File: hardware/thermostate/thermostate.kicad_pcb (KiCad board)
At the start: 2 copper layers, 80 x 80 mm, 28 parts, among them IC1 L8050QLT1G, IC2 L8050QLT1G, P1 USB_C_Plug_USB2.0, SW1 SW_Push, SW2 SW_Push, U1 ESP32-S3-WROOM-1, U2 LM1117-3.3

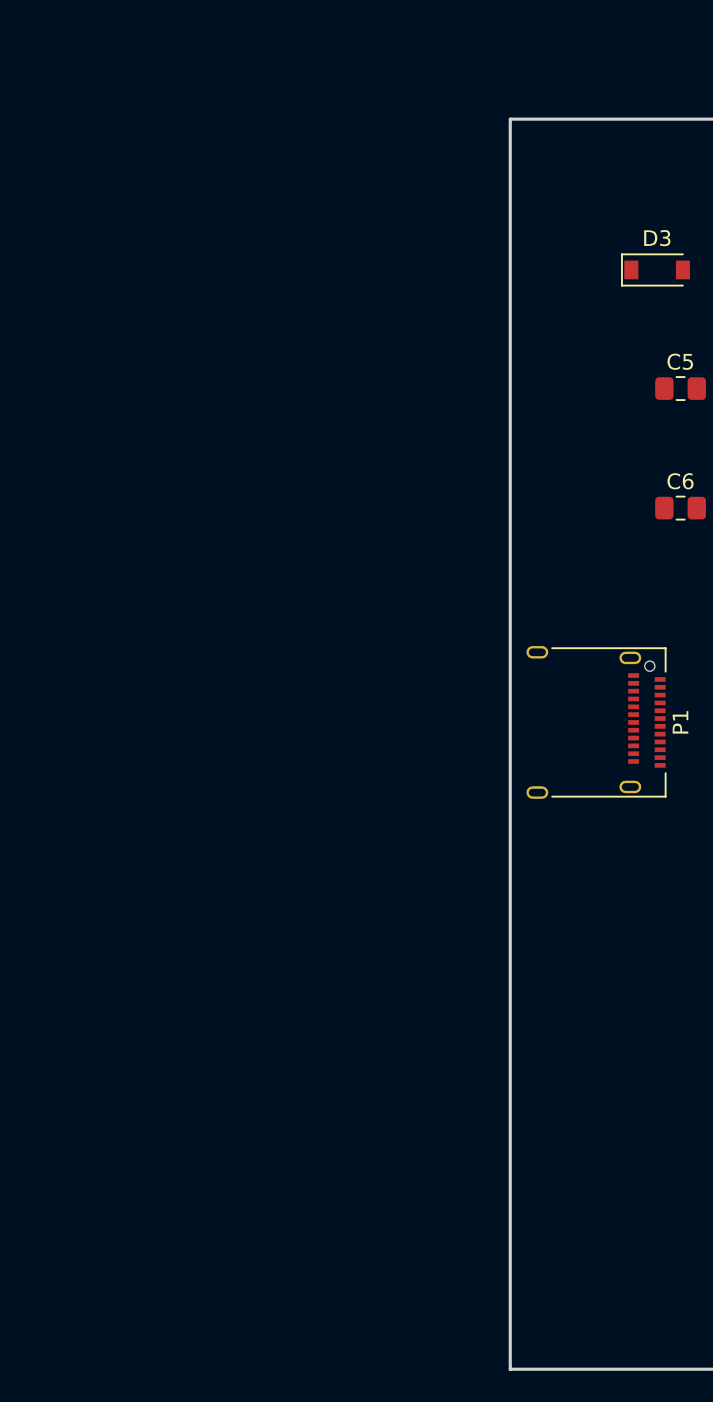
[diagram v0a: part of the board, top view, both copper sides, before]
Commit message: Add temperature sensor
Signed-off-by: Javier <javierfernandezvillasante@gmail.com>
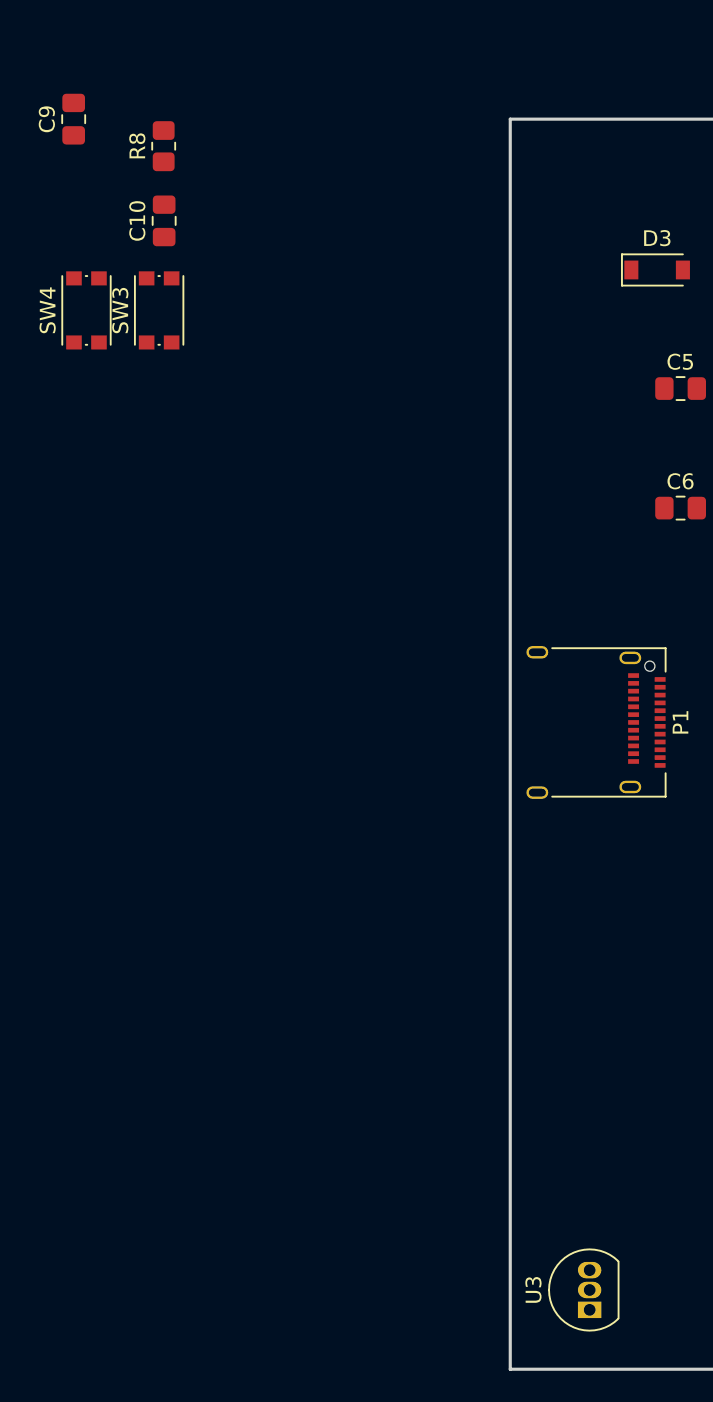
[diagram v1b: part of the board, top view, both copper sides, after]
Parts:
- added C10: 0.1uF/50V(20%), Capacitor_SMD:C_0805_2012Metric_Pad1.18x1.45mm_HandSolder, F.Cu at (84.5, 59.9)
- added C9: 0.1uF/50V(20%), Capacitor_SMD:C_0805_2012Metric_Pad1.18x1.45mm_HandSolder, F.Cu at (78.7, 53.3)
- added R8: 4K7(20%), Resistor_SMD:R_0805_2012Metric_Pad1.20x1.40mm_HandSolder, F.Cu at (84.5, 55.1)
- added SW3: SW_Push, Button_Switch_SMD:SW_Push_1P1T_NO_CK_KMR2, F.Cu at (84.2, 65.6)
- added SW4: SW_Push, Button_Switch_SMD:SW_Push_1P1T_NO_CK_KMR2, F.Cu at (79.6, 65.6)
- added U3: DS18B20, Package_TO_SOT_THT:TO-92_Inline, F.Cu at (111.8, 129.5)
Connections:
- net GND renamed PAD_-_ExternalPush_1
- U1 pad 16: unconnected-(U1-Pad16) -> TemperatureSensor
- U1 pad 23: unconnected-(U1-Pad23) -> ExternalPush_1
- U1 pad 26: unconnected-(U1-Pad26) -> ExternalPush_2

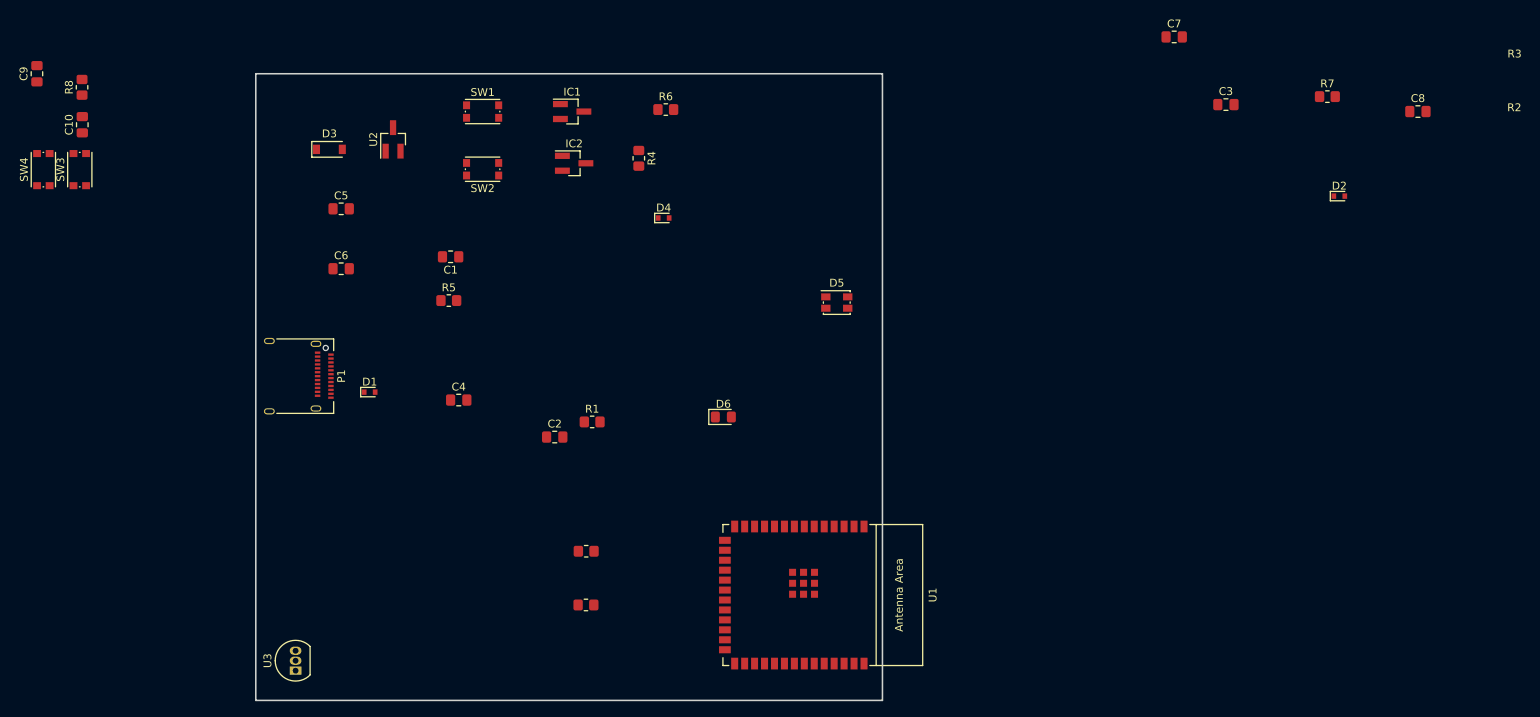
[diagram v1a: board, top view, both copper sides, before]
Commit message: Add Components PCB
Signed-off-by: Javier <javierfernandezvillasante@gmail.com>
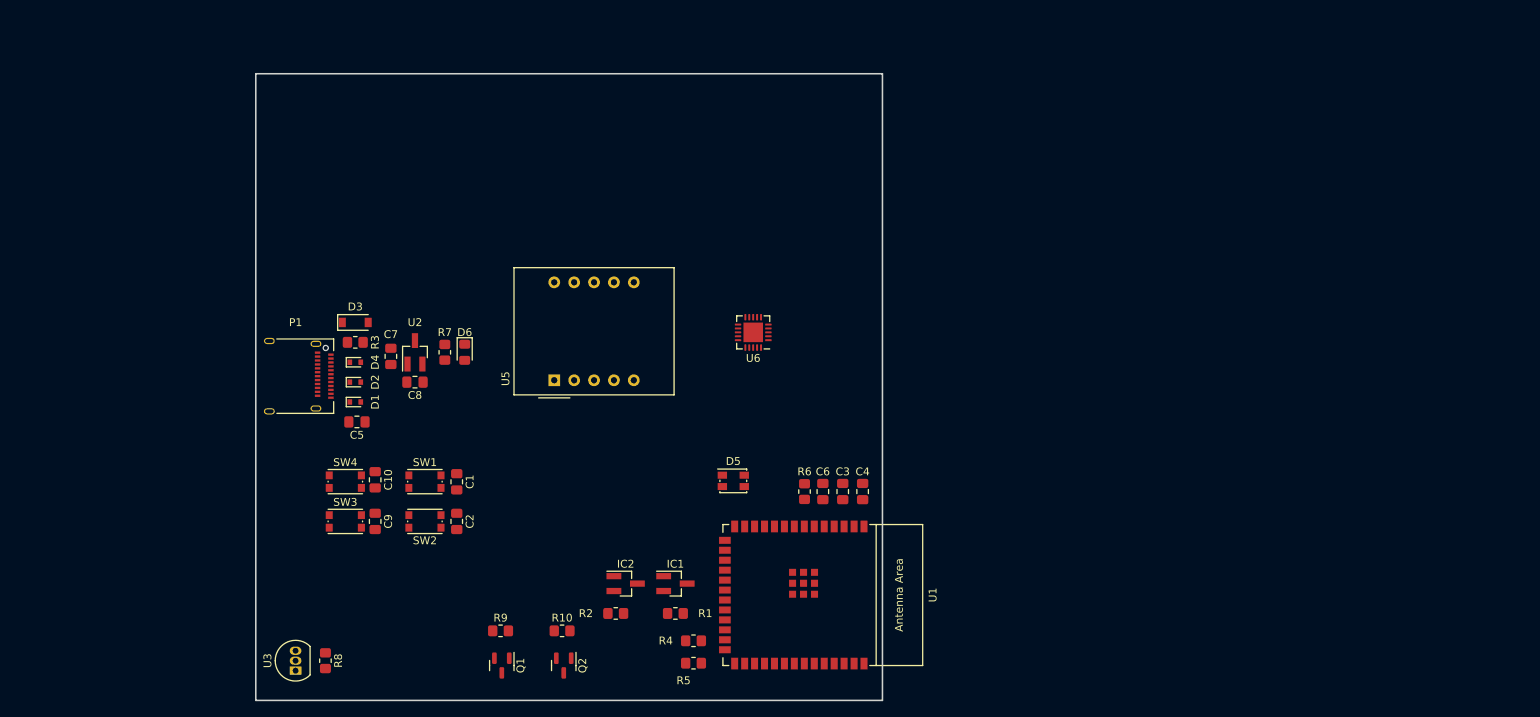
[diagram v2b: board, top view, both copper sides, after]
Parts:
- added Q1: BC847, Package_TO_SOT_SMD:SOT-23, F.Cu at (138.1, 128.9)
- added Q2: BC847, Package_TO_SOT_SMD:SOT-23, F.Cu at (146.0, 128.9)
- added R10: 10k (1%), Resistor_SMD:R_0805_2012Metric_Pad1.20x1.40mm_HandSolder, F.Cu at (145.8, 124.5)
- added R9: 10k (1%), Resistor_SMD:R_0805_2012Metric_Pad1.20x1.40mm_HandSolder, F.Cu at (137.9, 124.5)
- added U5: ELD-426SYGWA, Display_7Segment:ELD_426XXXX, F.Cu at (144.8, 92.5)
- added U6: ULN2803A, Package_DFN_QFN:QFN-20-1EP_4x4mm_P0.5mm_EP2.5x2.5mm, F.Cu at (170.2, 86.4)
- moved C8 132.6 mm to (127.0, 92.7), turned to 180 degrees
- moved D2 127.8 mm to (119.4, 92.7)
- moved R7 117.3 mm to (130.8, 88.9), turned to -90 degrees
- moved C7 108.0 mm to (123.9, 89.4), turned to -90 degrees
- moved R8 79.5 mm to (115.6, 128.3), turned to -90 degrees
- moved C9 71.6 mm to (121.9, 110.5), turned to -90 degrees
- moved C3 69.5 mm to (181.6, 106.7), turned to 90 degrees
- moved C6 67.8 mm to (179.1, 106.7), turned to 90 degrees
- moved R4 62.0 mm to (162.6, 125.7), turned to 180 degrees
- moved IC1 61.7 mm to (160.2, 118.4)
- moved C10 58.8 mm to (121.9, 105.2), turned to -90 degrees
- moved SW3 56.3 mm to (118.1, 110.5), turned to 0 degrees
- moved R5 55.8 mm to (162.6, 128.6), turned to 180 degrees
- moved SW4 55.4 mm to (118.1, 105.4), turned to 0 degrees
- moved IC2 54.1 mm to (153.9, 118.4)
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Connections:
- U1 pad 10: unconnected-(U1-Pad10) -> 7SEG_G
- U1 pad 11: unconnected-(U1-Pad11) -> 7SEG_DP
- U1 pad 19: unconnected-(U1-Pad19) -> 7SEG_A
- U1 pad 20: unconnected-(U1-Pad20) -> 7SEG_B
- U1 pad 21: unconnected-(U1-Pad21) -> 7SEG_C
- U1 pad 22: unconnected-(U1-Pad22) -> 7SEG_D
- U1 pad 36: unconnected-(U1-Pad36) -> 7SEG_2Controller
- U1 pad 37: unconnected-(U1-Pad37) -> 7SEG_1Controller
- U1 pad 8: unconnected-(U1-Pad8) -> 7SEG_E
- U1 pad 9: unconnected-(U1-Pad9) -> 7SEG_F

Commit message: Start desing PCB
Signed-off-by: Javier <javierfernandezvillasante@gmail.com>
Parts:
- added J1: Conn_01x02_Male, TerminalBlock_MetzConnect:TerminalBlock_MetzConnect_360291_1x01_Horizontal_ScrewM3.0_Boxed, F.Cu at (234.9, 45.7)
- added J2: Conn_01x02_Male, TerminalBlock_MetzConnect:TerminalBlock_MetzConnect_360291_1x01_Horizontal_ScrewM3.0_Boxed, F.Cu at (246.0, 45.7)
- added K1: SRD-03VDC-SL-C, SRD-03VDC-SL-C:SRD03VDCSLC, F.Cu at (214.2, 39.6)
- added R11: RK09K1130A5R, RK09K1130A5R:RK09K1130A5R, F.Cu at (240.0, 31.3)
- moved R4 22.6 mm to (174.7, 106.7), turned to 90 degrees
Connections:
- net GPIO19 renamed /ESP32_minimal/USB_N
- net GPIO20 renamed /ESP32_minimal/USB_P
- C1 pad 1: PAD_-_ExternalPush_1 -> GND
- C10 pad 1: PAD_-_ExternalPush_1 -> GND
- C2 pad 1: PAD_-_ExternalPush_1 -> GND
- C3 pad 2: PAD_-_ExternalPush_1 -> GND
- C4 pad 2: PAD_-_ExternalPush_1 -> GND
- C5 pad 2: PAD_-_ExternalPush_1 -> GND
- C6 pad 2: PAD_-_ExternalPush_1 -> GND
- C7 pad 2: PAD_-_ExternalPush_1 -> GND
- C8 pad 2: PAD_-_ExternalPush_1 -> GND
- C9 pad 1: PAD_-_ExternalPush_1 -> GND
- D1 pad 1: PAD_-_ExternalPush_1 -> GND
- D2 pad 1: PAD_-_ExternalPush_1 -> GND
- D4 pad 1: PAD_-_ExternalPush_1 -> GND
- D5 pad 2: PAD_-_ExternalPush_1 -> GND
- D6 pad 1: PAD_-_ExternalPush_1 -> GND
- P1 pad A1: PAD_-_ExternalPush_1 -> GND
- P1 pad A12: PAD_-_ExternalPush_1 -> GND
- P1 pad B1: PAD_-_ExternalPush_1 -> GND
- P1 pad B12: PAD_-_ExternalPush_1 -> GND
- P1 pad S1: PAD_-_ExternalPush_1 -> GND
- R3 pad 2: PAD_-_ExternalPush_1 -> GND
- SW1 pad 1: PAD_-_ExternalPush_1 -> GND
- SW2 pad 1: PAD_-_ExternalPush_1 -> GND
- SW3 pad 1: PAD_-_ExternalPush_1 -> ExternalPush_1
- SW4 pad 1: PAD_-_ExternalPush_1 -> Net-(SW4-Pad1)
- U1 pad 1: PAD_-_ExternalPush_1 -> GND
- U1 pad 40: PAD_-_ExternalPush_1 -> GND
- U1 pad 41: PAD_-_ExternalPush_1 -> GND
- U2 pad 1: PAD_-_ExternalPush_1 -> GND
- U3 pad 1: PAD_-_ExternalPush_1 -> GND
- U6 pad 9: PAD_-_ExternalPush_1 -> GND
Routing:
- net DTR: track 0.00 -> 12.7 mm
- net RTS: track 0.00 -> 6.30 mm
- net GPIO0: track 0.00 -> 4.28 mm

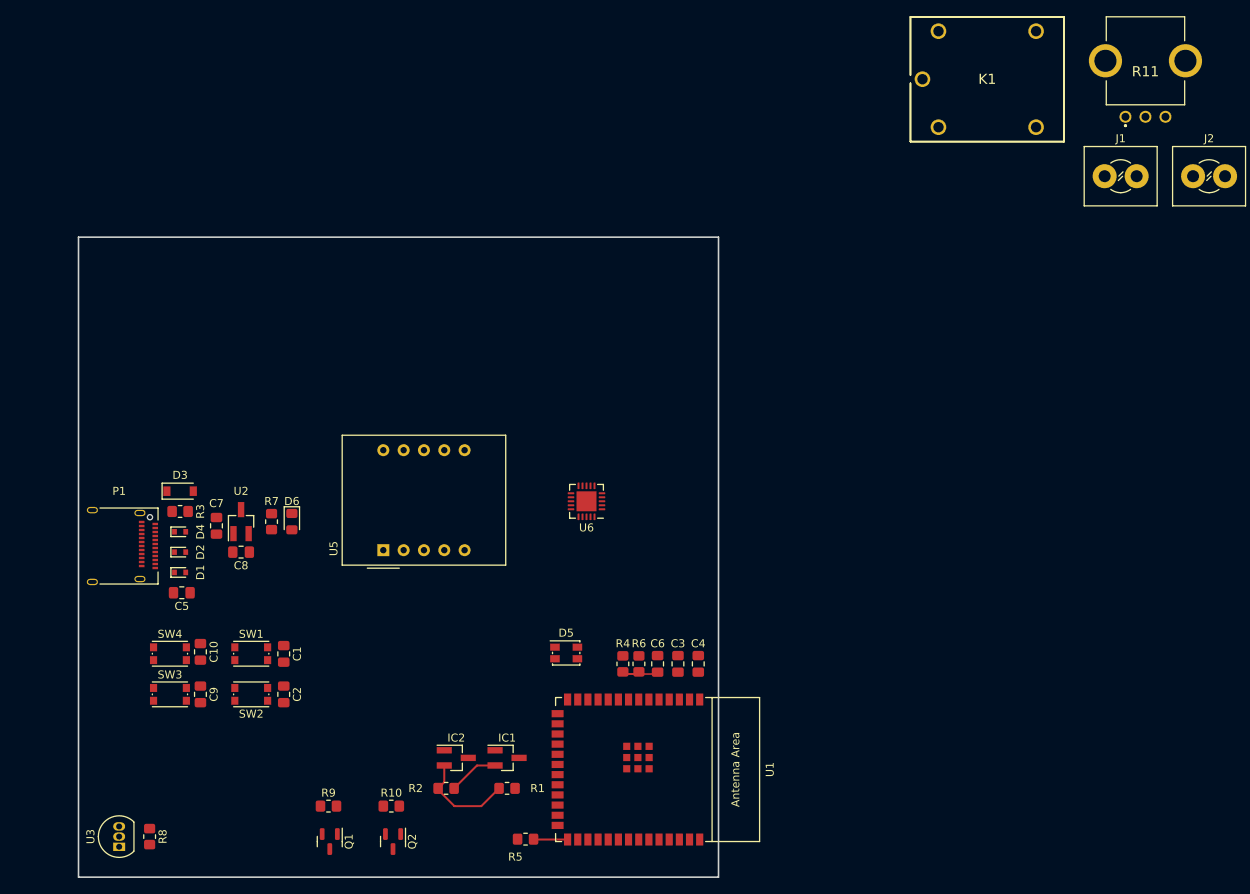
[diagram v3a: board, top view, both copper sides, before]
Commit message: Add First lines PCB
Signed-off-by: Javier <javierfernandezvillasante@gmail.com>
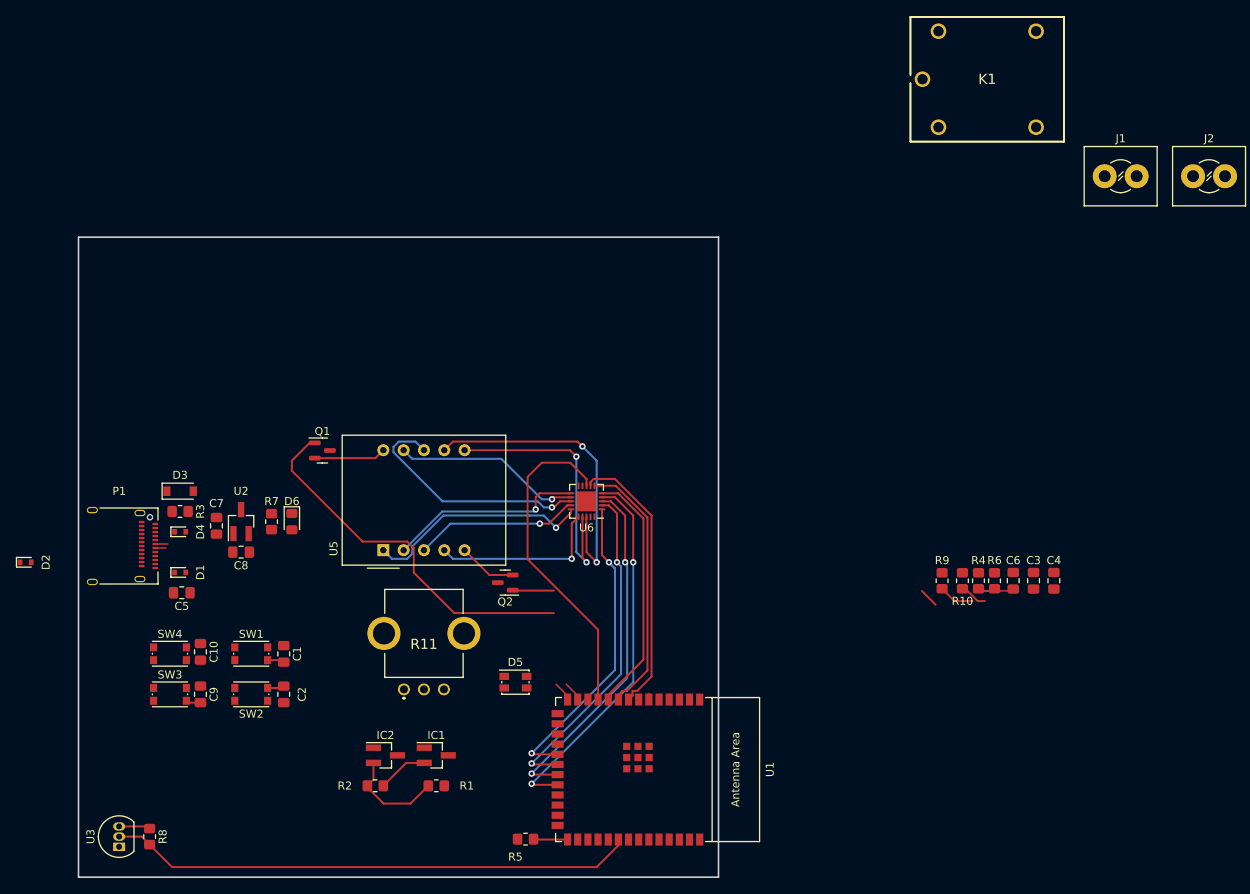
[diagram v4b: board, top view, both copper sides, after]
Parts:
- moved R11 115.1 mm to (149.9, 102.9)
- moved R9 81.7 mm to (214.6, 96.3), turned to 90 degrees
- moved R10 76.7 mm to (217.2, 96.3), turned to 90 degrees
- moved Q1 48.9 mm to (137.2, 80.0), turned to 0 degrees
- moved C6 45.6 mm to (223.5, 96.3)
- moved R4 45.6 mm to (219.2, 96.3)
- moved R6 45.6 mm to (221.2, 96.3)
- moved C3 45.6 mm to (226.1, 96.3)
- moved C4 45.6 mm to (228.6, 96.3)
- moved Q2 35.3 mm to (160.0, 96.5), turned to 180 degrees
- moved D2 19.3 mm to (100.1, 94.0)
- moved IC1 8.86 mm to (151.4, 118.1)
- moved IC2 8.86 mm to (145.1, 118.1)
- moved R1 8.86 mm to (151.4, 121.9)
- moved R2 8.86 mm to (143.8, 121.9)
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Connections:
- U1 pad 10: 7SEG_G -> 7SEG_E
- U1 pad 16: TemperatureSensor -> unconnected-(U1-Pad16)
- U1 pad 32: unconnected-(U1-Pad32) -> TemperatureSensor
- U1 pad 36: 7SEG_2Controller -> unconnected-(U1-Pad36)
- U1 pad 37: 7SEG_1Controller -> unconnected-(U1-Pad37)
- U1 pad 6: unconnected-(U1-Pad6) -> 7SEG_2Controller
- U1 pad 7: unconnected-(U1-Pad7) -> 7SEG_1Controller
- U1 pad 8: 7SEG_E -> 7SEG_G
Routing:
- net TemperatureSensor: track 0.00 -> 65.8 mm
- net Net-(Q1-Pad1): track 0.00 -> 47.0 mm
- net 7SEG_D: track 0.00 -> 46.9 mm, vias 0 -> 2
- net 7SEG_C: track 0.00 -> 44.2 mm, vias 0 -> 2
- net 7SEG_B: track 0.00 -> 41.7 mm, vias 0 -> 2
- net 7SEG_DP: track 0.00 -> 41.3 mm
- net Net-(U5-Pad7): track 0.00 -> 39.4 mm, vias 0 -> 2
- net 7SEG_A: track 0.00 -> 38.8 mm, vias 0 -> 2
- net 7SEG_G: track 0.00 -> 34.7 mm
- net Net-(U5-Pad6): track 0.00 -> 33.9 mm, vias 0 -> 2
- net 7SEG_E: track 0.00 -> 33.6 mm
- net 7SEG_F: track 0.00 -> 32.9 mm
- net Net-(U5-Pad8): track 0.00 -> 30.6 mm, vias 0 -> 1
- net Net-(U5-Pad1): track 0.00 -> 28.8 mm, vias 0 -> 1
- net Net-(U5-Pad2): track 0.00 -> 24.8 mm, vias 0 -> 1
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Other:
- copper layers 2 -> 4
